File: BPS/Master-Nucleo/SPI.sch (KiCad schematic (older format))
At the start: 51 parts, among them J10 DisplayJumper, J7 VoltageSlaveConnector, J8 DisplayConnector, J9 TempSlaveConnector, U10 LTC6820, U11 HX1188FNL, U12 LTC6820, U13 Si8641EC-B-IS1, U14 SI8660EC-B-IS1, U15 RI3-1205S

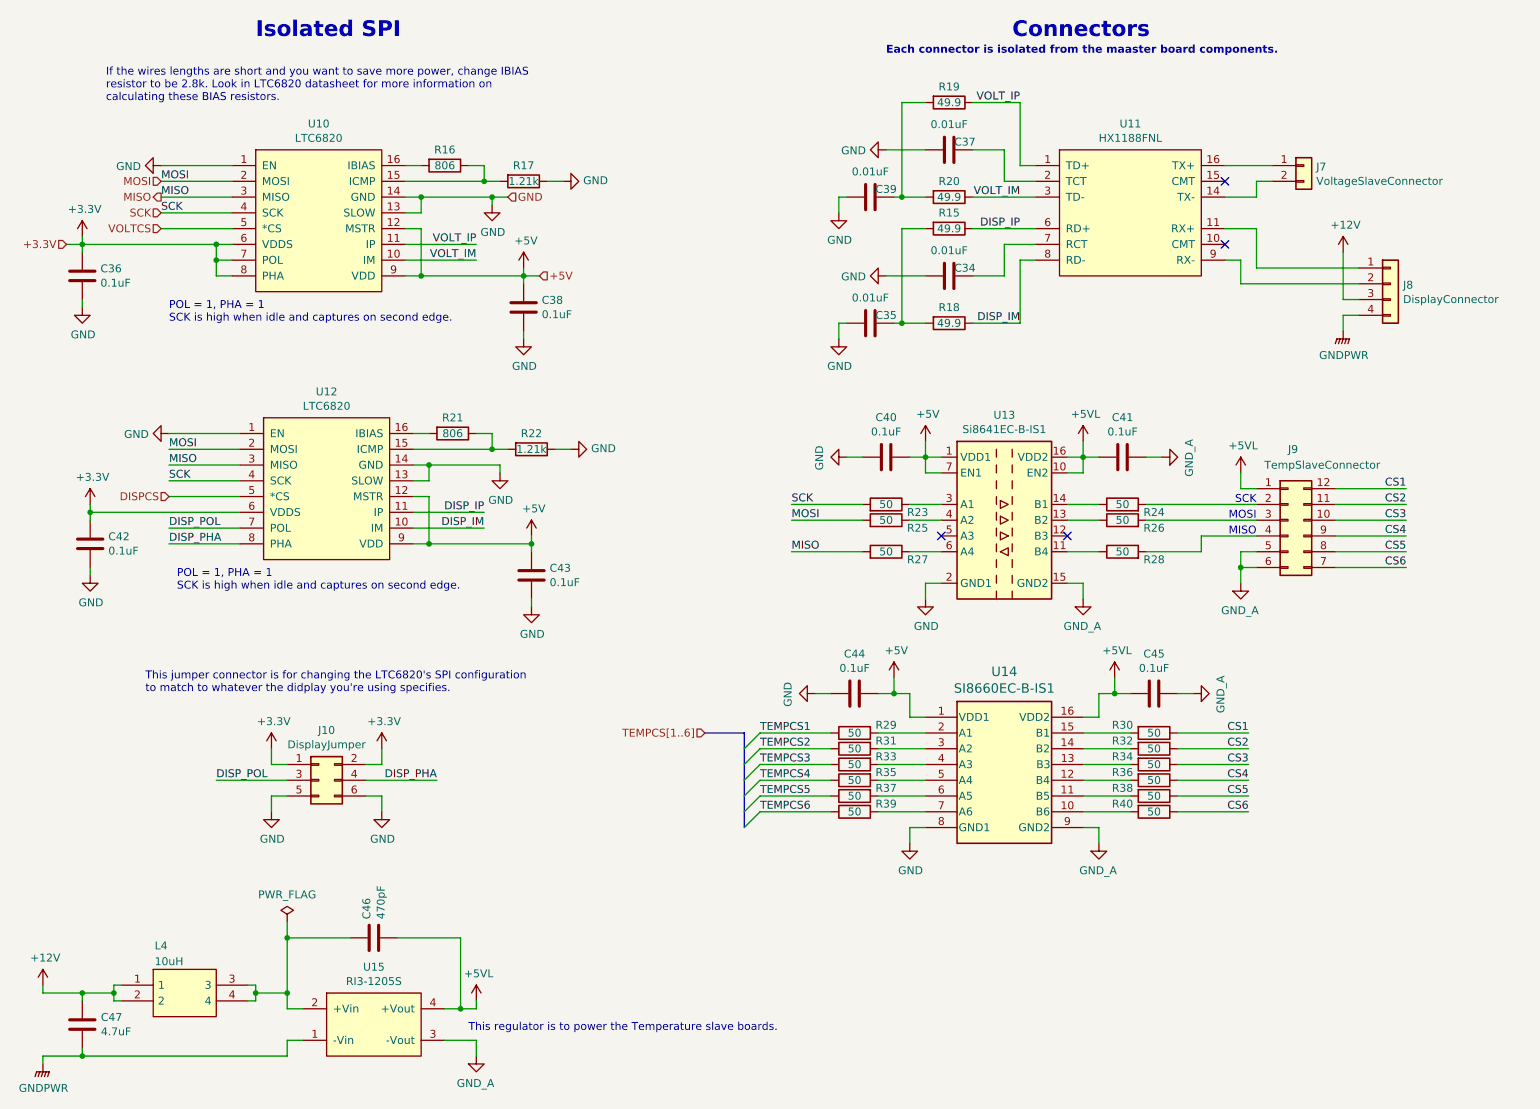
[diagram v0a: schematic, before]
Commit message: Adds Nucleo version of master board.
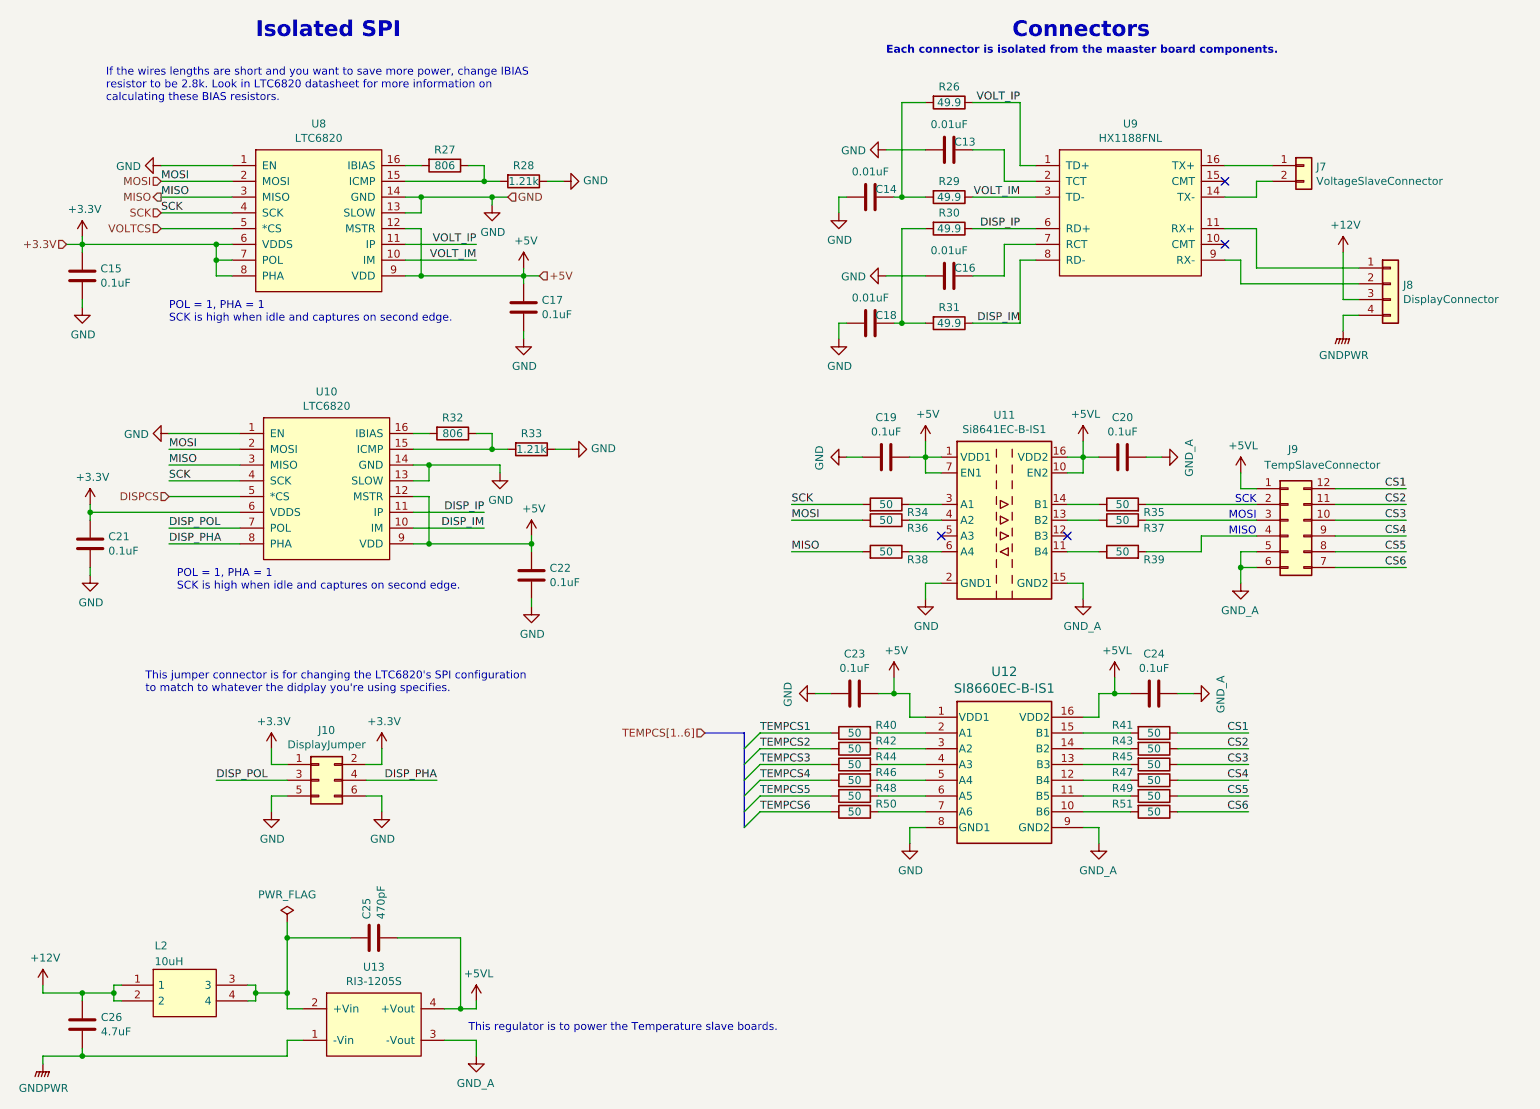
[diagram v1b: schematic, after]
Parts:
- renumbered C37 to C13, C39 to C14, C36 to C15, C34 to C16, C38 to C17, C35 to C18, C40 to C19, C41 to C20, C42 to C21, C43 to C22, C44 to C23, C45 to C24, R19 to R26, R16 to R27, R17 to R28, R20 to R29, R15 to R30, R18 to R31, R21 to R32, R22 to R33, R23 to R34, R24 to R35, R25 to R36, R26 to R37, R27 to R38, R28 to R39, R29 to R40, R30 to R41, R31 to R42, R32 to R43, R33 to R44, R34 to R45, R35 to R46, R36 to R47, R37 to R48, R38 to R49, R39 to R50, R40 to R51, U12 to U10, U13 to U11, U14 to U12, U10 to U8, U11 to U9

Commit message: worked on pcb layout and schematic
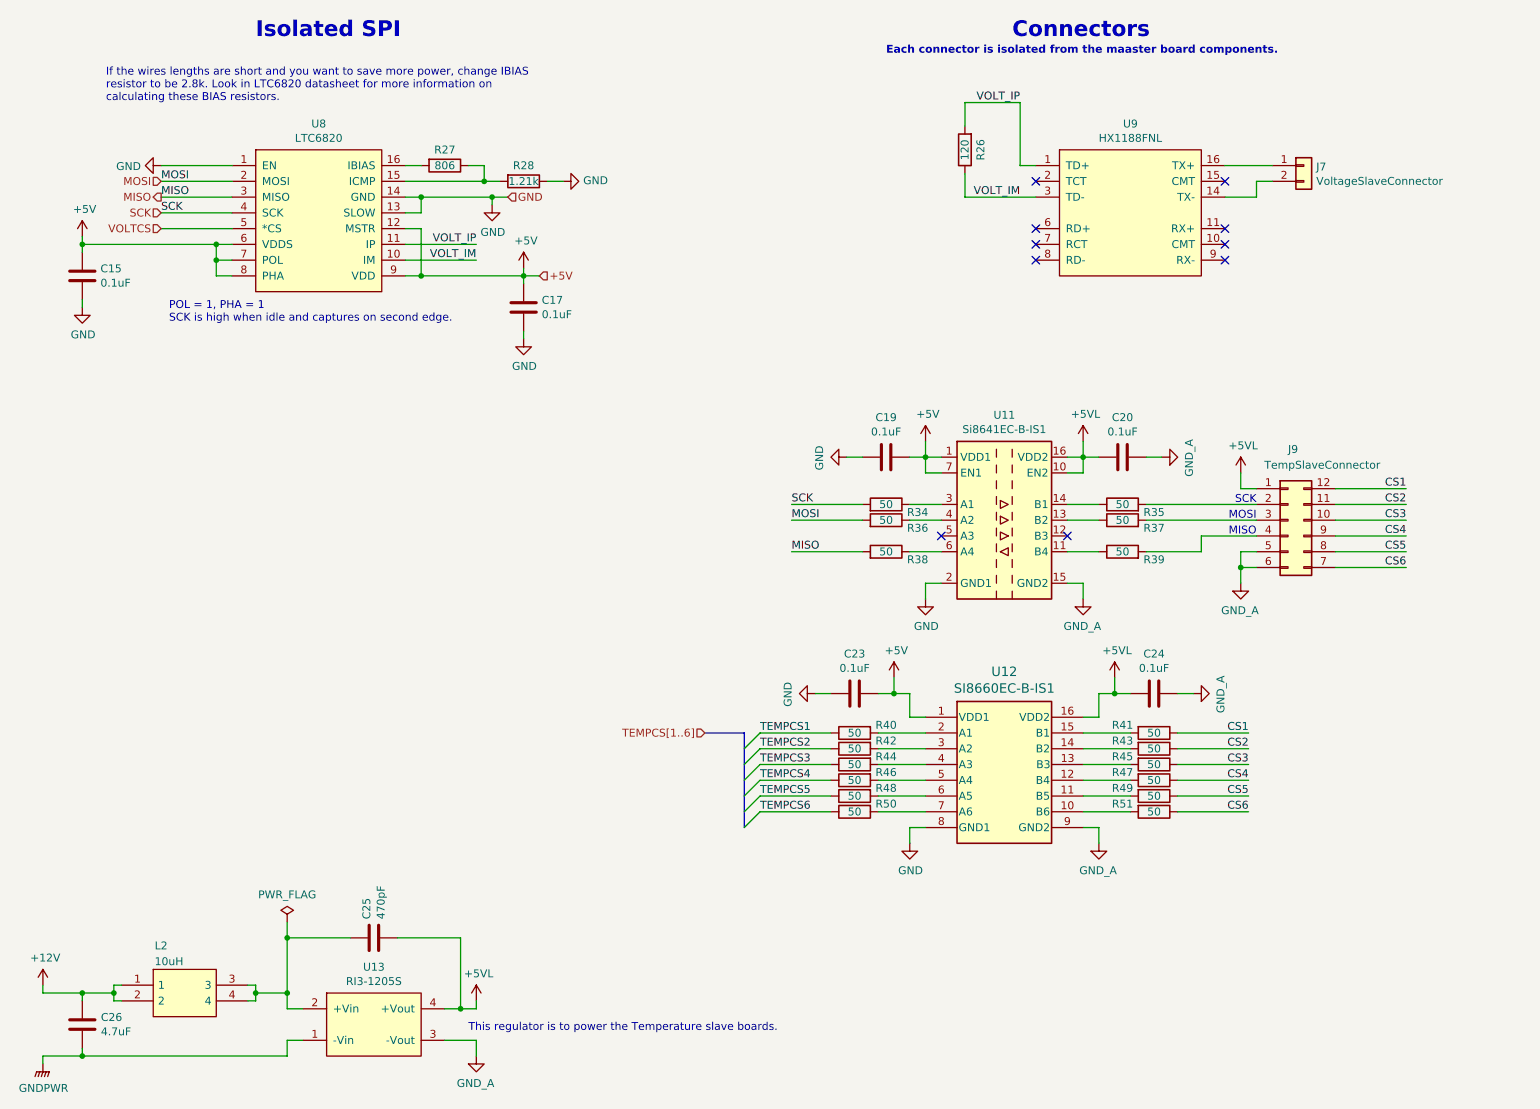
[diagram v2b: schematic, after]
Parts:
- removed C13, C14, C16, C18: 0.01uF, Capacitor_SMD:C_0805_2012Metric, symbol Device:C
- removed C21, C22: 0.1uF, Capacitor_SMD:C_0805_2012Metric, symbol Device:C
- removed J10: DisplayJumper, Connector_PinHeader_2.54mm:PinHeader_2x03_P2.54mm_Vertical, symbol Connector_Generic:Conn_02x03_Odd_Even
- removed J8: DisplayConnector, UTSVT_Connectors:Molex_MicroFit3.0_1x4xP3.00mm_PolarizingPeg_Vertical, symbol Connector_Generic:Conn_01x04
- removed R29, R30, R31: 49.9, Resistor_SMD:R_0805_2012Metric, symbol Device:R
- removed R32: 806, Resistor_SMD:R_0805_2012Metric, symbol Device:R
- removed R33: 1.21k, Resistor_SMD:R_0805_2012Metric, symbol Device:R
- removed U10: LTC6820, Package_SO:MSOP-16_3x4mm_P0.5mm, symbol utsvt-bps:LTC6820
- R26: value 49.9 -> 120
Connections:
- net +3V3 is gone; now on net +5V: C15.1, U8.6 (VDDS), U8.7 (POL), U8.8 (PHA)
- net VOLT_IM: now also R26.1
- net VOLT_IP: now also R26.2; no longer R26.1
- net DISP_IM: no longer names the net of U9.8 (RD-)
- net DISP_IP: no longer names the net of U9.6 (RD+)
- no-connect marks 4 -> 10
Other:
- note removed: "This jumper connector is for changing the LTC6820's SPI configuration\nto match to whatever the didplay you're using specifies."
- moved on the sheet: R26
